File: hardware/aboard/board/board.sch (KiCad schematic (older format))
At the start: 25 parts, among them P1 Power, P2 Analog, P3 Digital, P4 Digital, P5 CONN_01X01, P6 CONN_01X01, P7 CONN_01X01, P8 CONN_01X01, U1 24LC512, U10 ST25DV04K, U2 AT25SF081-SSHD-X, U3 24LC512, U4 AT25SF081-SSHD-X, U5 24LC512, U6 LTC3406ES5, U8 Si5351A, U9 ICE40UP5K-SG48ITR, Y1 Crystal

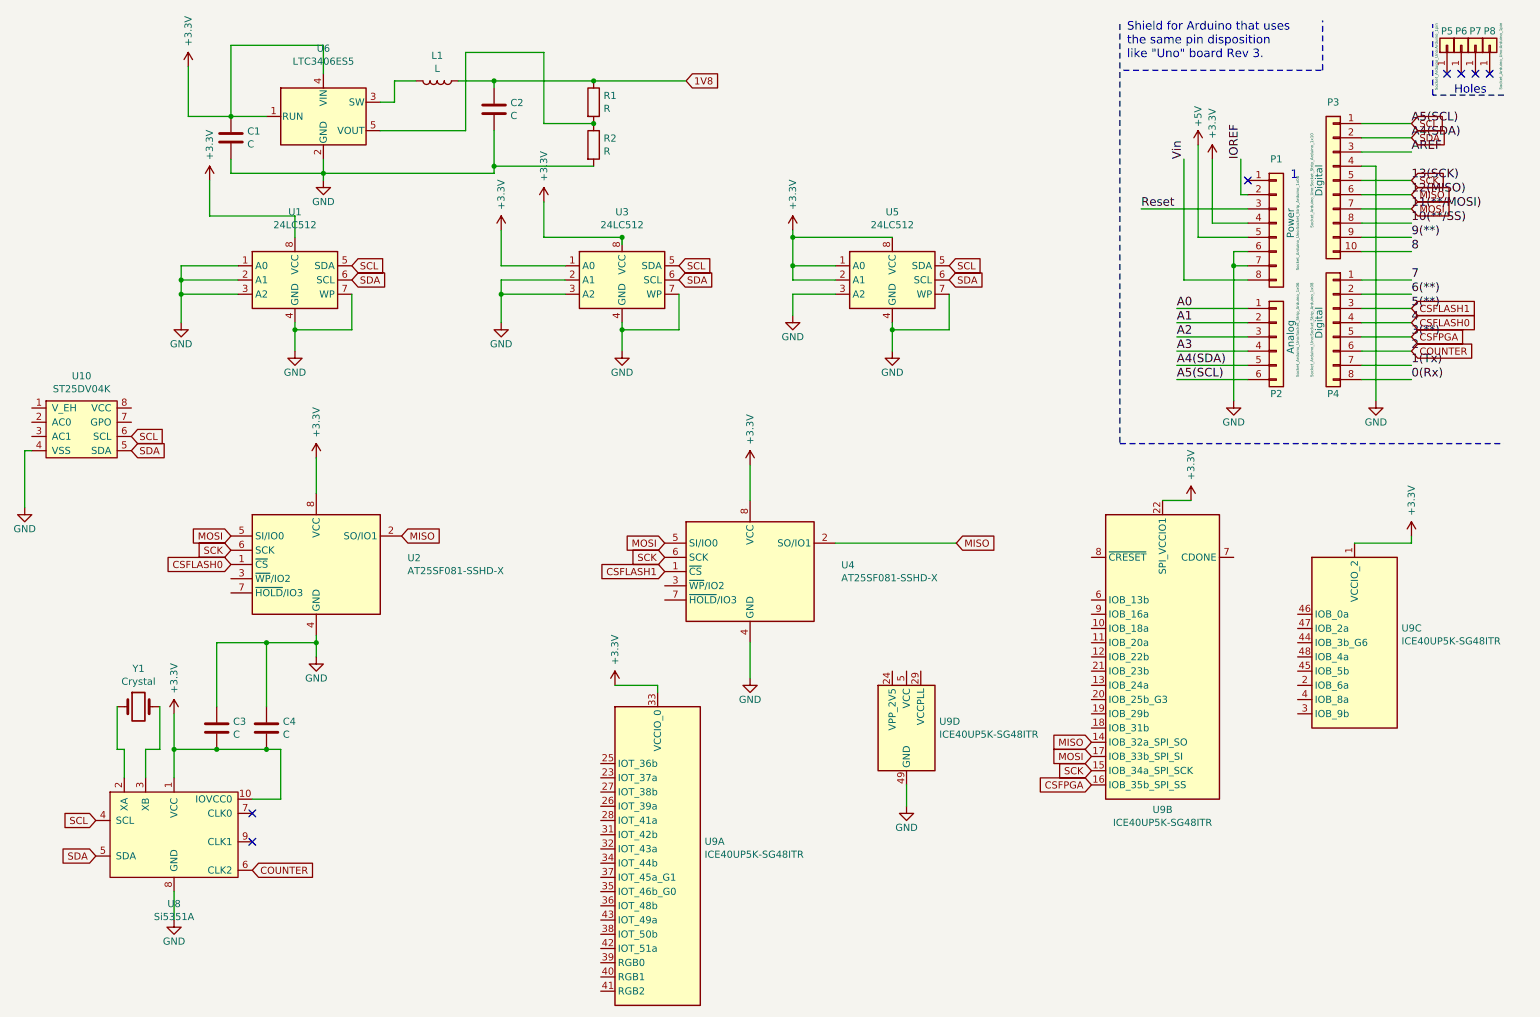
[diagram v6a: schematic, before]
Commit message: board for OM13088UL: process 2
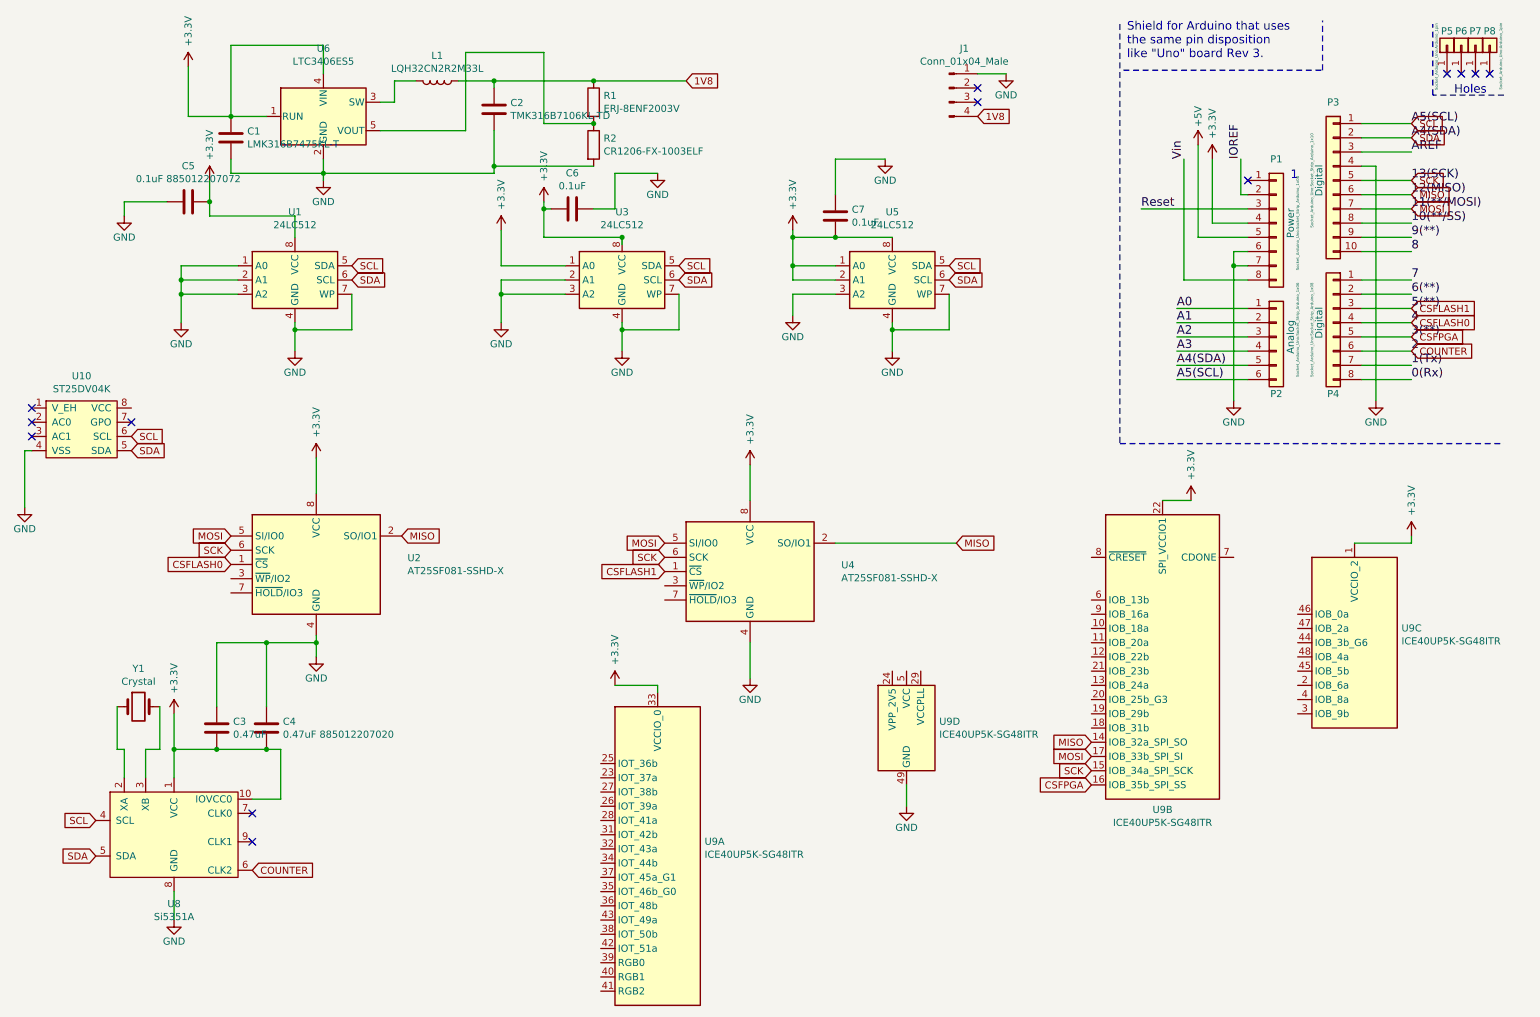
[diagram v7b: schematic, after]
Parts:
- added C5: 0.1uF 885012207072, Capacitor_SMD:C_0805_2012Metric, symbol Device:C
- added C6, C7: 0.1uF, Capacitor_SMD:C_0805_2012Metric, symbol Device:C
- added J1: Conn_01x04_Male, Connector_PinHeader_2.54mm:PinHeader_1x04_P2.54mm_Vertical, symbol Connector:Conn_01x04_Male
- C1: value C -> LMK316B7475KL-T; footprint (none) -> Capacitor_SMD:C_1206_3216Metric
- C2: value C -> TMK316B7106KL-TD; footprint (none) -> Capacitor_SMD:C_1206_3216Metric
- C3: value C -> 0.47uF; footprint (none) -> Capacitor_SMD:C_0805_2012Metric
- C4: value C -> 0.47uF 885012207020; footprint (none) -> Capacitor_SMD:C_0805_2012Metric
- L1: value L -> LQH32CN2R2M33L; footprint (none) -> Inductor_SMD:L_1210_3225Metric
- R1: value R -> ERJ-8ENF2003V; footprint (none) -> Resistor_SMD:R_1206_3216Metric
- R2: value R -> CR1206-FX-1003ELF; footprint (none) -> Resistor_SMD:R_1206_3216Metric
- Y1: footprint (none) -> Crystal:Crystal_SMD_5032-2Pin_5.0x3.2mm
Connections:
- net +3V3: now also C5.1, C6.2, C7.1
- net 1V8: now also J1.4 (Pin_4)
- net GND: now also C5.2, C6.1, C7.2, J1.1 (Pin_1)
- no-connect marks 7 -> 13
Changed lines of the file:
@@
 $EndComp
 Wire Wire Line
-	2100 1600 2100 1850
+	2100 1600 2100 1750
 $Comp
 L power:+3.3V #PWR010
@@
 $EndComp
 Wire Wire Line
-	4450 1750 4450 2000
+	4450 1750 4450 1800
 Wire Wire Line
 	2100 1850 2700 1850
@@
 	4450 2000 5000 2000
 Wire Wire Line
-	6200 2000 6900 2000
+	6200 2000 6500 2000
 Connection ~ 6200 2000
 Wire Wire Line
@@
 P 2250 1300
 F 0 "C1" H 2365 1346 50  0000 L CNN
-F 1 "C" H 2365 1255 50  0000 L CNN
-F 2 "" H 2288 1150 50  0001 C CNN
+F 1 " LMK316B7475KL-T " H 2365 1255 50  0000 L CNN
+F 2 "Capacitor_SMD:C_1206_3216Metric" H 2288 1150 50  0001 C CNN
 F 3 "~" H 2250 1300 50  0001 C CNN
 	1    2250 1300
@@
 P 3700 900
 F 0 "L1" V 3522 900 50  0000 C CNN
-F 1 "L" V 3613 900 50  0000 C CNN
-F 2 "" H 3700 900 50  0001 C CNN
+F 1 "LQH32CN2R2M33L" V 3613 900 50  0000 C CNN
+F 2 "Inductor_SMD:L_1210_3225Metric" H 3700 900 50  0001 C CNN
 F 3 "~" H 3700 900 50  0001 C CNN
 	1    3700 900
@@
 P 4100 1100
 F 0 "C2" H 4215 1146 50  0000 L CNN
-F 1 "C" H 4215 1055 50  0000 L CNN
-F 2 "" H 4138 950 50  0001 C CNN
+F 1 " TMK316B7106KL-TD " H 4215 1055 50  0000 L CNN
+F 2 "Capacitor_SMD:C_1206_3216Metric" H 4138 950 50  0001 C CNN
 F 3 "~" H 4100 1100 50  0001 C CNN
 	1    4100 1100
@@
 P 4800 1050
 F 0 "R1" H 4870 1096 50  0000 L CNN
-F 1 "R" H 4870 1005 50  0000 L CNN
-F 2 "" V 4730 1050 50  0001 C CNN
+F 1 " ERJ-8ENF2003V " H 4870 1005 50  0000 L CNN
+F 2 "Resistor_SMD:R_1206_3216Metric" V 4730 1050 50  0001 C CNN
 F 3 "~" H 4800 1050 50  0001 C CNN
 	1    4800 1050
@@
 P 4800 1350
 F 0 "R2" H 4870 1396 50  0000 L CNN
-F 1 "R" H 4870 1305 50  0000 L CNN
-F 2 "" V 4730 1350 50  0001 C CNN
+F 1 " CR1206-FX-1003ELF" H 4870 1305 50  0000 L CNN
+F 2 "Resistor_SMD:R_1206_3216Metric" V 4730 1350 50  0001 C CNN
 F 3 "~" H 4800 1350 50  0001 C CNN
 	1    4800 1350
@@
 F 0 "Y1" H 1600 5568 50  0000 C CNN
 F 1 "Crystal" H 1600 5477 50  0000 C CNN
-F 2 "" H 1600 5300 50  0001 C CNN
+F 2 "Crystal:Crystal_SMD_5032-2Pin_5.0x3.2mm" H 1600 5300 50  0001 C CNN
 F 3 "~" H 1600 5300 50  0001 C CNN
 	1    1600 5300
@@
 P 2150 5450
 F 0 "C3" H 2265 5496 50  0000 L CNN
-F 1 "C" H 2265 5405 50  0000 L CNN
-F 2 "" H 2188 5300 50  0001 C CNN
+F 1 "0.47uF" H 2265 5405 50  0000 L CNN
+F 2 "Capacitor_SMD:C_0805_2012Metric" H 2188 5300 50  0001 C CNN
 F 3 "~" H 2150 5450 50  0001 C CNN
 	1    2150 5450
@@
 P 2500 5450
 F 0 "C4" H 2615 5496 50  0000 L CNN
-F 1 "C" H 2615 5405 50  0000 L CNN
-F 2 "" H 2538 5300 50  0001 C CNN
+F 1 "0.47uF 885012207020" H 2615 5405 50  0000 L CNN
+F 2 "Capacitor_SMD:C_0805_2012Metric" H 2538 5300 50  0001 C CNN
 F 3 "~" H 2500 5450 50  0001 C CNN
 	1    2500 5450
@@
 CSFLASH1
 $Comp
-L power:+3.3V #PWR?
+L power:+3.3V #PWR030
 U 1 1 5D467BB4
 P 10550 4100
-F 0 "#PWR?" H 10550 3950 50  0001 C CNN
+F 0 "#PWR030" H 10550 3950 50  0001 C CNN
 F 1 "+3.3V" V 10550 4350 50  0000 C CNN
 F 2 "" H 10550 4100 50  0000 C CNN
@@
 $EndComp
 $Comp
-L power:+3.3V #PWR?
+L power:+3.3V #PWR029
 U 1 1 5D46CD35
 P 9000 3850
-F 0 "#PWR?" H 9000 3700 50  0001 C CNN
+F 0 "#PWR029" H 9000 3700 50  0001 C CNN
 F 1 "+3.3V" V 9000 4100 50  0000 C CNN
 F 2 "" H 9000 3850 50  0000 C CNN
@@
 $EndComp
 $Comp
-L power:+3.3V #PWR?
+L power:+3.3V #PWR025
 U 1 1 5D471EB6
 P 4950 5150
-F 0 "#PWR?" H 4950 5000 50  0001 C CNN
+F 0 "#PWR025" H 4950 5000 50  0001 C CNN
 F 1 "+3.3V" V 4950 5400 50  0000 C CNN
 F 2 "" H 4950 5150 50  0000 C CNN
@@
 CSFLASH1
 $Comp
-L power:+3.3V #PWR?
+L power:+3.3V #PWR027
 U 1 1 5D487BC5
 P 5900 3600
-F 0 "#PWR?" H 5900 3450 50  0001 C CNN
+F 0 "#PWR027" H 5900 3450 50  0001 C CNN
 F 1 "+3.3V" V 5900 3850 50  0000 C CNN
 F 2 "" H 5900 3600 50  0000 C CNN
@@
 $EndComp
 $Comp
-L power:+3.3V #PWR?
+L power:+3.3V #PWR024
 U 1 1 5D48D267
 P 2850 3550
-F 0 "#PWR?" H 2850 3400 50  0001 C CNN
+F 0 "#PWR024" H 2850 3400 50  0001 C CNN
 F 1 "+3.3V" V 2850 3800 50  0000 C CNN
 F 2 "" H 2850 3550 50  0000 C CNN
@@
 Wire Wire Line
 	2850 3550 2850 3800
+$Comp
+L Device:C C5
+U 1 1 5D49E0A8
+P 1950 1750
+F 0 "C5" V 1698 1750 50  0000 C CNN
+F 1 "0.1uF 885012207072 " V 1789 1750 50  0000 C CNN
+F 2 "Capacitor_SMD:C_0805_2012Metric" H 1988 1600 50  0001 C CNN
+F 3 "~" H 1950 1750 50  0001 C CNN
+	1    1950 1750
+	0    1    1    0
+$EndComp
+Connection ~ 2100 1750
+Wire Wire Line
+	2100 1750 2100 1850
+$Comp
+L Device:C C6
+U 1 1 5D49E18B
+P 4650 1800
+F 0 "C6" V 4398 1800 50  0000 C CNN
+F 1 "0.1uF" V 4489 1800 50  0000 C CNN
+F 2 "Capacitor_SMD:C_0805_2012Metric" H 4688 1650 50  0001 C CNN
+F 3 "~" H 4650 1800 50  0001 C CNN
+	1    4650 1800
+	0    1    1    0
+$EndComp
+Wire Wire Line
+	4450 1800 4500 1800
+Connection ~ 4450 1800
+Wire Wire Line
+	4450 1800 4450 2000
+$Comp
+L Device:C C7
+U 1 1 5D4A3D97
+P 6500 1850
+F 0 "C7" H 6385 1804 50  0000 R CNN
+F 1 "0.1uF" H 6385 1895 50  0000 R CNN
+F 2 "Capacitor_SMD:C_0805_2012Metric" H 6538 1700 50  0001 C CNN
+F 3 "~" H 6500 1850 50  0001 C CNN
+	1    6500 1850
+	-1   0    0    1
+$EndComp
+Connection ~ 6500 2000
+Wire Wire Line
+	6500 2000 6900 2000
+$Comp
+L power:GND #PWR028
+U 1 1 5D4A3EA5
+P 6850 1450
+F 0 "#PWR028" H 6850 1200 50  0001 C CNN
+F 1 "GND" H 6850 1300 50  0000 C CNN
+F 2 "" H 6850 1450 50  0000 C CNN
+F 3 "" H 6850 1450 50  0000 C CNN
+	1    6850 1450
+	1    0    0    -1
+$EndComp
+$Comp
+L power:GND #PWR026
+U 1 1 5D4A9C3D
+P 5250 1550
+F 0 "#PWR026" H 5250 1300 50  0001 C CNN
+F 1 "GND" H 5250 1400 50  0000 C CNN
+F 2 "" H 5250 1550 50  0000 C CNN
+F 3 "" H 5250 1550 50  0000 C CNN
+	1    5250 1550
+	1    0    0    -1
+$EndComp
+$Comp
+L power:GND #PWR023
+U 1 1 5D4AF9D5
+P 1500 1850
+F 0 "#PWR023" H 1500 1600 50  0001 C CNN
+F 1 "GND" H 1500 1700 50  0000 C CNN
+F 2 "" H 1500 1850 50  0000 C CNN
+F 3 "" H 1500 1850 50  0000 C CNN
+	1    1500 1850
+	1    0    0    -1
+$EndComp
+Wire Wire Line
+	1500 1850 1500 1750
+Wire Wire Line
+	1500 1750 1800 1750
+Wire Wire Line
+	4800 1800 4950 1800
+Wire Wire Line
+	4950 1800 4950 1550
+Wire Wire Line
+	4950 1550 5250 1550
+Wire Wire Line
+	6500 1700 6500 1450
+Wire Wire Line
+	6500 1450 6850 1450
+$Comp
+L Connector:Conn_01x04_Male J1
+U 1 1 5D4CAB57
+P 7300 950
+F 0 "J1" H 7406 1228 50  0000 C CNN
+F 1 "Conn_01x04_Male" H 7406 1137 50  0000 C CNN
+F 2 "Connector_PinHeader_2.54mm:PinHeader_1x04_P2.54mm_Vertical" H 7300 950 50  0001 C CNN
+F 3 "~" H 7300 950 50  0001 C CNN
+	1    7300 950
+	1    0    0    -1
+$EndComp
+$Comp
+L power:GND #PWR031
+U 1 1 5D4CB004
+P 7700 850
+F 0 "#PWR031" H 7700 600 50  0001 C CNN
+F 1 "GND" H 7700 700 50  0000 C CNN
+F 2 "" H 7700 850 50  0000 C CNN
+F 3 "" H 7700 850 50  0000 C CNN
+	1    7700 850
+	1    0    0    -1
+$EndComp
+Text GLabel 7500 1150 2    50   Input ~ 0
+1V8
+Wire Wire Line
+	7500 850  7700 850
+NoConn ~ 7500 950
+NoConn ~ 7500 1050
+NoConn ~ 1550 3300
+NoConn ~ 850  3200
+NoConn ~ 850  3300
+NoConn ~ 850  3400
 $EndSCHEMATC

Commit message: board for OM13088UL: process 3
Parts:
- removed U5: 24LC512, symbol Memory_EEPROM:24LC512
- added C10, C11, C12, C13, C14, C15, C16, C17: 0.1uF, Capacitor_SMD:C_0805_2012Metric, symbol Device:C
- added C8: LMK316B7475KL-T, Capacitor_SMD:C_1206_3216Metric, symbol Device:C
- added C9: 0.1uF 885012207072, Capacitor_SMD:C_0805_2012Metric, symbol Device:C
- added R3, R4: R, Resistor_SMD:R_1206_3216Metric, symbol Device:R
- added U5: 24LC512, Package_DFN_QFN:DFN-8-1EP_6x5mm_P1.27mm_EP4x4mm, symbol kilib2:24LC512
- U1, U10: footprint (none) -> Package_SO:TSSOP-8_4.4x3mm_P0.65mm
- U3: footprint (none) -> Package_SO:SOIC-8_3.9x4.9mm_P1.27mm
- U8: footprint (none) -> Package_SO:MSOP-10_3x3mm_P0.5mm
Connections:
- net 6(**) is gone; now on net CDONE: P4.2 (Pin_2)
- net 7 is gone; now on net CRESET: P4.1 (Pin_1)
- net +3V3: now also U10.8 (VCC), U2.7 (~HOLD~/IO3), U4.7 (~HOLD~/IO3), U9.24 (VPP_2V5), C10.2, C11.1, C12.2, C15.2, C16.2, C17.2, C8.1, C9.2, R3.2, R4.2, U5.1 (A0), U5.2 (A1), U5.8 (VCC)
- net 1V8: now also U9.29 (VCCPLL), U9.30 (VCC), U9.5 (VCC), C13.2, C14.2
- net GND: now also C10.1, C11.2, C12.1, C13.1, C14.1, C15.1, C16.1, C17.1, C8.2, C9.1, U5.3 (A2), U5.4 (GND), U5.7 (WP), U5.9 (EP)
- net SCL: now also U5.5 (SDA); no longer P2.6 (Pin_6)
- net SDA: now also U5.6 (SCL); no longer P2.5 (Pin_5)
- net at U2.3 (~WP~/IO2): now also R3.1
- net at U4.3 (~WP~/IO2): now also R4.1
- net CDONE: now reaches U9.7 (CDONE)
- net CRESET: now reaches U9.8 (~CRESET)
- no-connect marks 13 -> 63
